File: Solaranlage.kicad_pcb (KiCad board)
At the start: 2 copper layers, 160 x 85 mm, 77 parts, among them J1 Screw_Terminal_01x02, J2 Screw_Terminal_01x02, J3 AVR-JTAG-10, J4 USB_B, J5 USB_B, J6 Screw_Terminal_01x02, Q1 2N3904, Q2 BC328, SW1 Rotary_Encoder_Switch_Panason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, SW2 SW_SPDT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

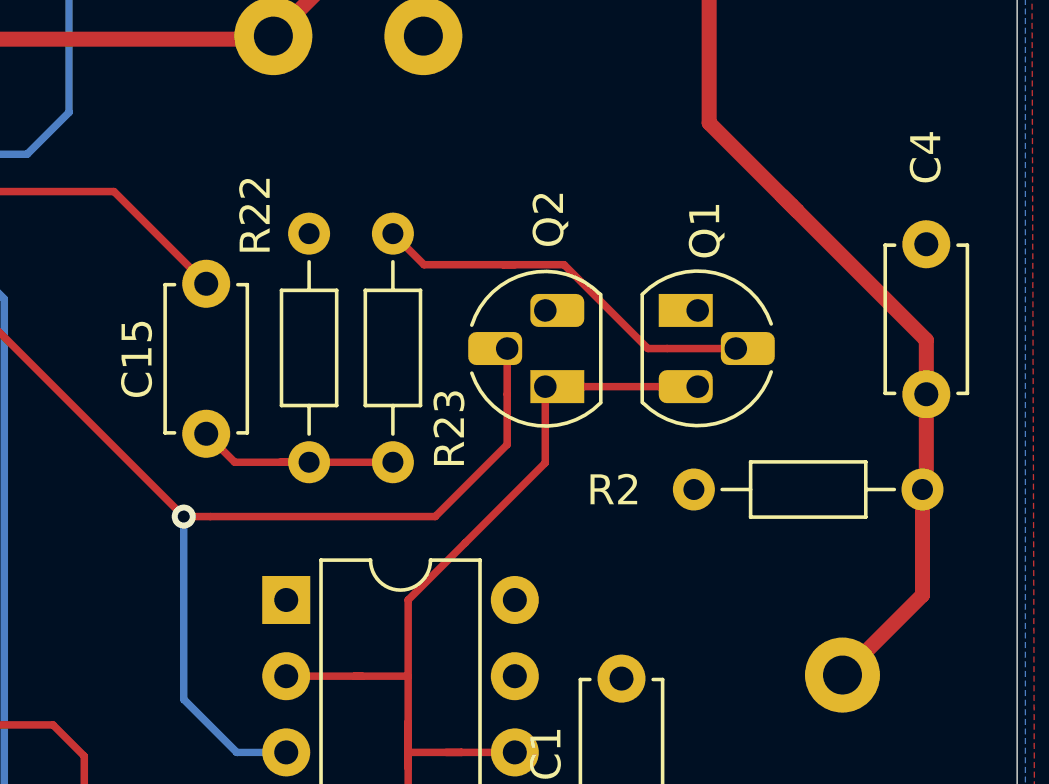
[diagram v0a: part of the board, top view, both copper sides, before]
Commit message: removed Q2. Had no plan why it was added. Inserted jumper to disable watchdog during sw-development
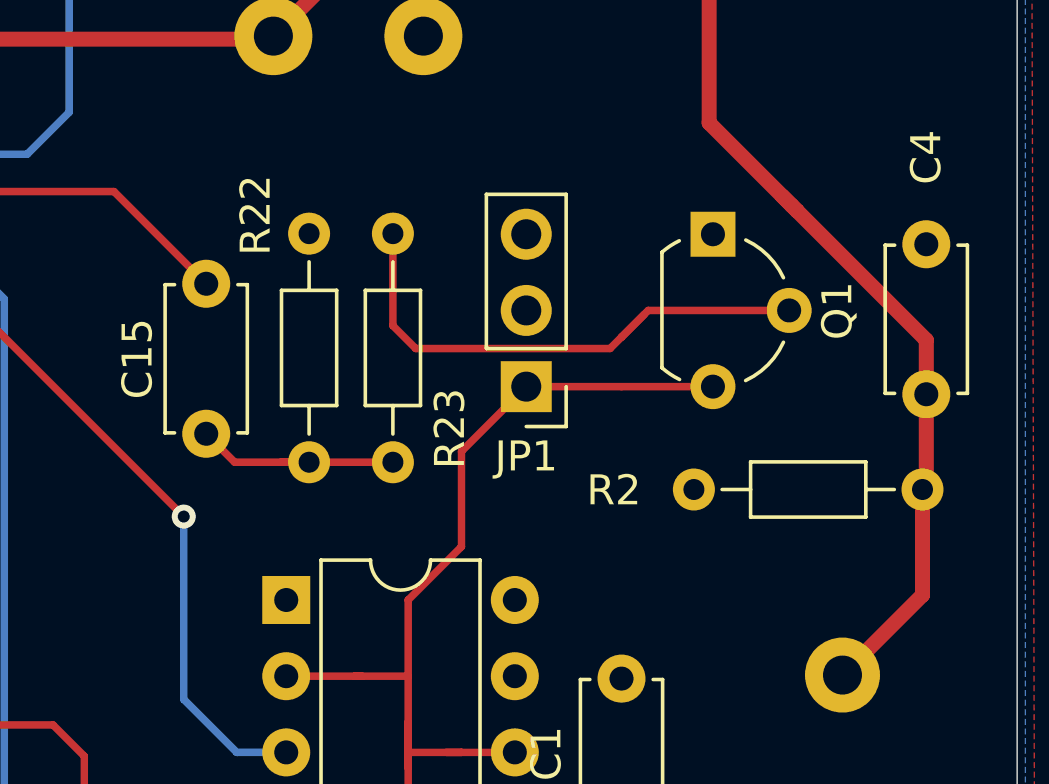
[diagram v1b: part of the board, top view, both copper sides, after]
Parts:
- removed Q2: BC328, Package_TO_SOT_THT:TO-92_HandSolder
- added JP1: Jumper, Connector_PinHeader_2.54mm:PinHeader_1x03_P2.54mm_Vertical, F.Cu at (212.7, 100.1)
- Q1: footprint Package_TO_SOT_THT:TO-92_HandSolder -> Package_TO_SOT_THT:TO-92L_Wide
- moved Q1 2.59 mm to (218.9, 95.0)
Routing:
- net \RST: track 214.0 -> 199.0 mm
- net Net-(Q1-Pad2): track 13.4 -> 18.2 mm

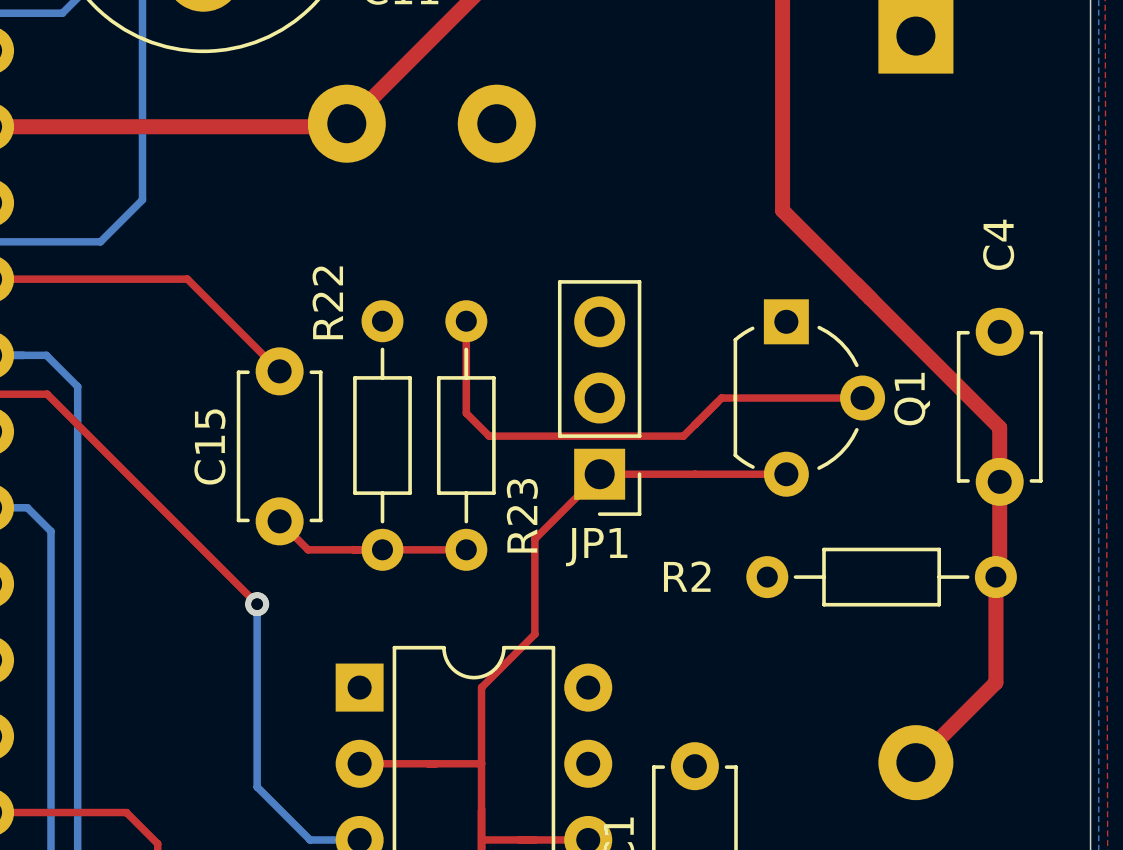
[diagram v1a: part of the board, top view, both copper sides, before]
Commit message: fixed frequency of crystal in schematic
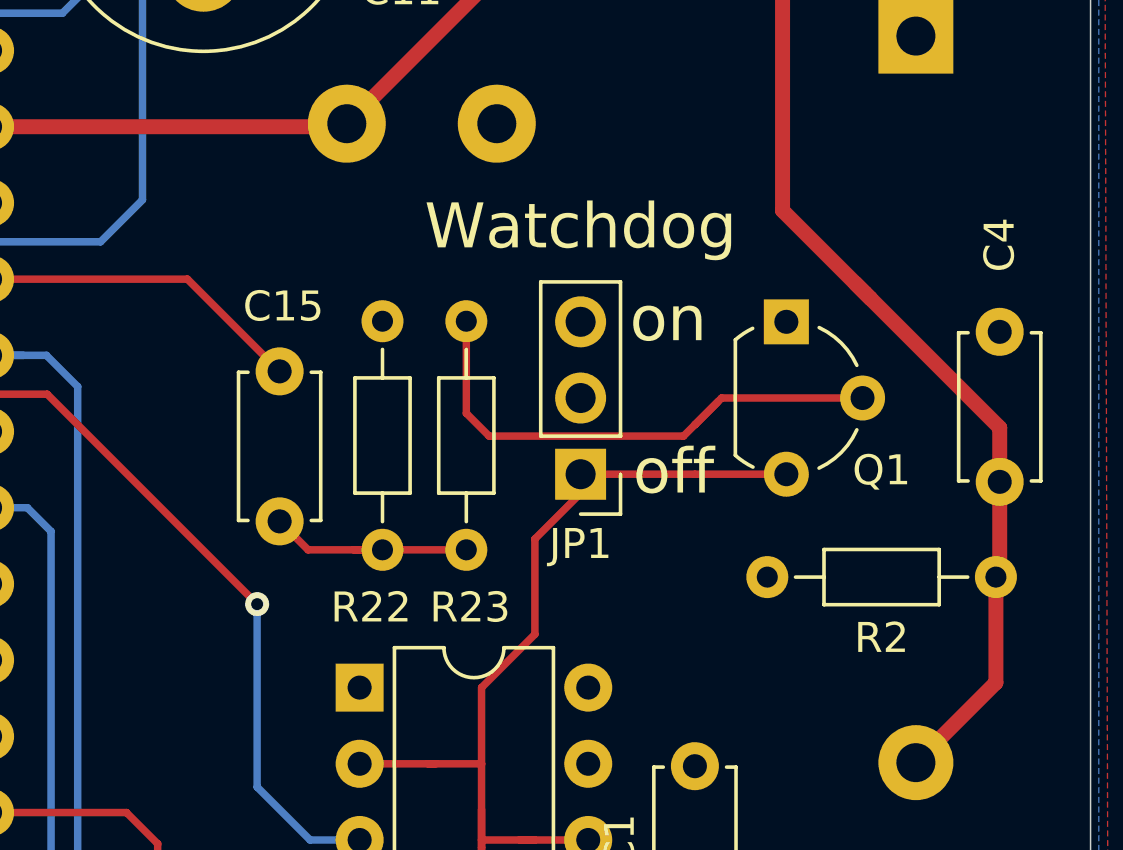
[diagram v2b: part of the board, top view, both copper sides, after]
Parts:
- moved JP1 0.63 mm to (212.1, 100.1)
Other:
- board text added: "Watchdog"
- board text added: "off"
- board text added: "on"
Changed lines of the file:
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@@
   (general
     (thickness 1.6)
-    (drawings 10)
+    (drawings 13)
     (tracks 755)
     (zones 0)
@@
     (descr "TO-92L leads in-line (large body variant of TO-92), also known as TO-226, wide, drill 0.75mm (see https://www.diodes.com/assets/Package-Files/TO92L.pdf and http://www.ti.com/lit/an/snoa059/snoa059.pdf)")
     (tags "TO-92L Molded Wide transistor")
-    (fp_text reference Q1 (at 2.55 -4.15 90) (layer F.SilkS)
+    (fp_text reference Q1 (at 4.953 -3.175 180) (layer F.SilkS)
       (effects (font (size 1 1) (thickness 0.15)))
     )
@@
   )
   (module Connector_PinHeader_2.54mm:PinHeader_1x03_P2.54mm_Vertical (layer F.Cu)
-    (at 212.725 100.076 180)
+    (at 212.09 100.076 180)
     (descr "Through hole straight pin header, 1x03, 2.54mm pitch, single row")
     (tags "Through hole pin header THT 1x03 2.54mm single row")
@@
     (descr "C, Disc series, Radial, pin pitch=5.00mm, , diameter*width=4.7*2.5mm^2, Capacitor, http://www.vishay.com/docs/45233/krseries.pdf")
     (tags "C Disc series Radial pin pitch 5.00mm  diameter 4.7mm width 2.5mm Capacitor")
-    (fp_text reference C15 (at 2.5 2.286 90) (layer F.SilkS)
+    (fp_text reference C15 (at -2.159 -0.127) (layer F.SilkS)
       (effects (font (size 1 1) (thickness 0.15)))
     )
@@
     (descr "Resistor, Axial_DIN0204 series, Axial, Horizontal, pin pitch=7.62mm, 0.167W, length*diameter=3.6*1.6mm^2, http://cdn-reichelt.de/documents/datenblatt/B400/1_4W%23YAG.pdf")
     (tags "Resistor Axial_DIN0204 series Axial Horizontal pin pitch 7.62mm 0.167W length 3.6mm diameter 1.6mm")
-    (fp_text reference R23 (at 1.123 1.905 90) (layer F.SilkS)
+    (fp_text reference R23 (at -1.925 0.127 180) (layer F.SilkS)
       (effects (font (size 1 1) (thickness 0.15)))
     )
@@
     (descr "Resistor, Axial_DIN0204 series, Axial, Horizontal, pin pitch=7.62mm, 0.167W, length*diameter=3.6*1.6mm^2, http://cdn-reichelt.de/documents/datenblatt/B400/1_4W%23YAG.pdf")
     (tags "Resistor Axial_DIN0204 series Axial Horizontal pin pitch 7.62mm 0.167W length 3.6mm diameter 1.6mm")
-    (fp_text reference R22 (at 8.235 -1.778 270) (layer F.SilkS)
+    (fp_text reference R22 (at -1.925 -0.381) (layer F.SilkS)
       (effects (font (size 1 1) (thickness 0.15)))
     )
@@
     (descr "Resistor, Axial_DIN0204 series, Axial, Horizontal, pin pitch=7.62mm, 0.167W, length*diameter=3.6*1.6mm^2, http://cdn-reichelt.de/documents/datenblatt/B400/1_4W%23YAG.pdf")
     (tags "Resistor Axial_DIN0204 series Axial Horizontal pin pitch 7.62mm 0.167W length 3.6mm diameter 1.6mm")
-    (fp_text reference R2 (at -2.667 0.031) (layer F.SilkS)
+    (fp_text reference R2 (at 3.81 2.032) (layer F.SilkS)
       (effects (font (size 1 1) (thickness 0.15)))
     )
@@
     )
   )
+  (gr_text off (at 215.189571 99.9935) (layer F.SilkS)
+    (effects (font (size 1.5 1.5) (thickness 0.15)))
+  )
+  (gr_text on (at 215.011 94.9135) (layer F.SilkS)
+    (effects (font (size 1.5 1.5) (thickness 0.15)))
+  )
+  (gr_text "Watchdog\n" (at 212.09 91.821) (layer F.SilkS)
+    (effects (font (size 1.5 1.5) (thickness 0.15)))
+  )
   (gr_text "gain Kessel" (at 216.281 69.596) (layer B.SilkS)
     (effects (font (size 1 1) (thickness 0.15)) (justify mirror))
@@
     (connect_pads (clearance 0.508))
     (min_thickness 0.254)
-    (fill yes (arc_segments 32) (thermal_gap 0.508) (thermal_bridge_width 0.508))
+    (fill (arc_segments 32) (thermal_gap 0.508) (thermal_bridge_width 0.508))
     (polygon
       (pts
@@
     (connect_pads (clearance 0.508))
     (min_thickness 0.254)
-    (fill yes (arc_segments 32) (thermal_gap 0.508) (thermal_bridge_width 0.508))
+    (fill (arc_segments 32) (thermal_gap 0.508) (thermal_bridge_width 0.508))
     (polygon
       (pts

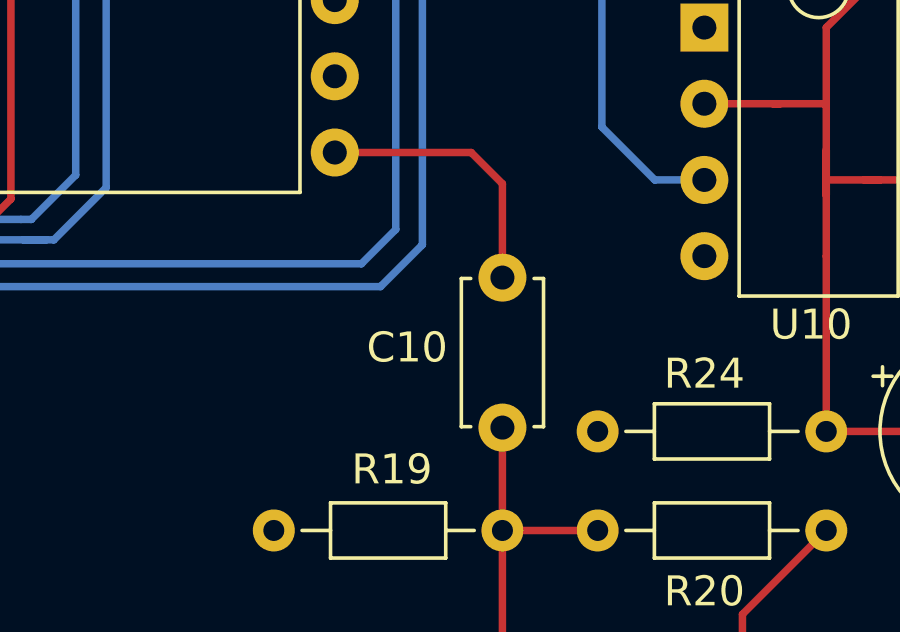
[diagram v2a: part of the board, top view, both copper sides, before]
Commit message: removed C10 (for common mode blocking of pwm in case of stalling output), because the pwm frequency had to be lowered to 30 Hz
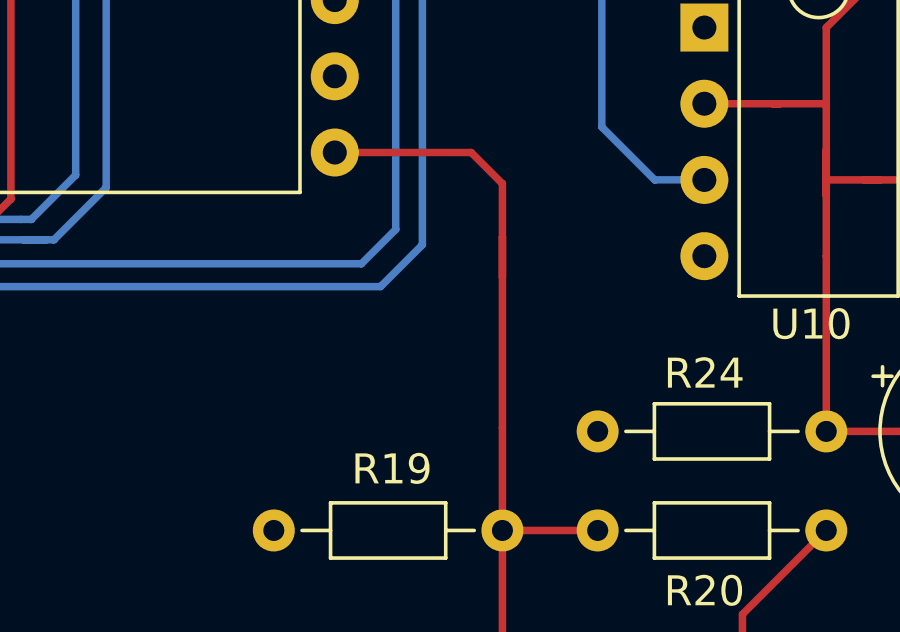
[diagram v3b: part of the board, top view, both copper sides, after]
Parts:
- removed C10: 10n, Capacitor_THT:C_Disc_D4.7mm_W2.5mm_P5.00mm
- Y1: value 8 Mhz -> 7.3728 Mhz
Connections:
- J6 pad 2: /PWM_2 -> /PWM
- R19 pad 1: /PWM_2 -> /PWM
- R20 pad 1: /PWM_2 -> /PWM
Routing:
- net /PWM: track 9.33 -> 30.4 mm
- net /PWM_2: track 14.9 -> 0.00 mm

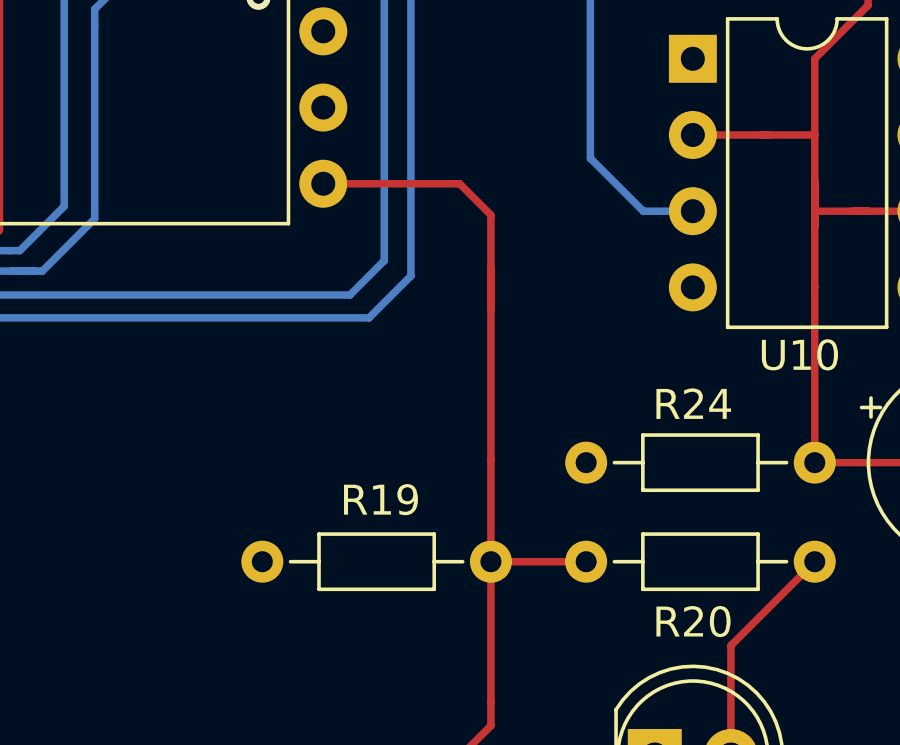
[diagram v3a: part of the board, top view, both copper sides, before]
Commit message: added 1k serial resistance in the PWM output line to protect GPIO PD7 from burning down
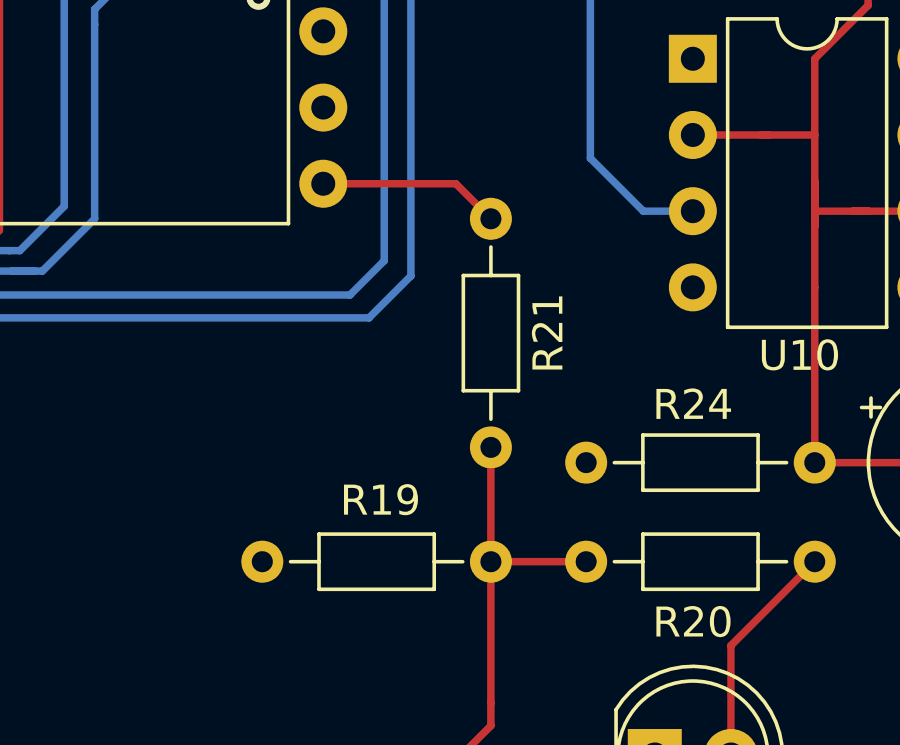
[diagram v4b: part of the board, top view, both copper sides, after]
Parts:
- added R21: 1k, Resistor_THT:R_Axial_DIN0204_L3.6mm_D1.6mm_P7.62mm_Horizontal, F.Cu at (198.0, 112.5)
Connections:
- U7 pad 21: /PWM -> Net-(R21-Pad1)
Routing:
- net /PWM: track 30.4 -> 15.3 mm
- net Net-(R21-Pad1): track 0.00 -> 6.07 mm
